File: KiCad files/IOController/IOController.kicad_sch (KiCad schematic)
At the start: 22 parts, among them J2 XT60 Horizontal Socket, J3 edge connector, Q1 BSS138, SW1 RotaryEncoder_Switch, SW2 B3U, U1 LP2985-1.8, U2 TLV75533PDBV, U3 LP2985-5.0, U4 RP2040

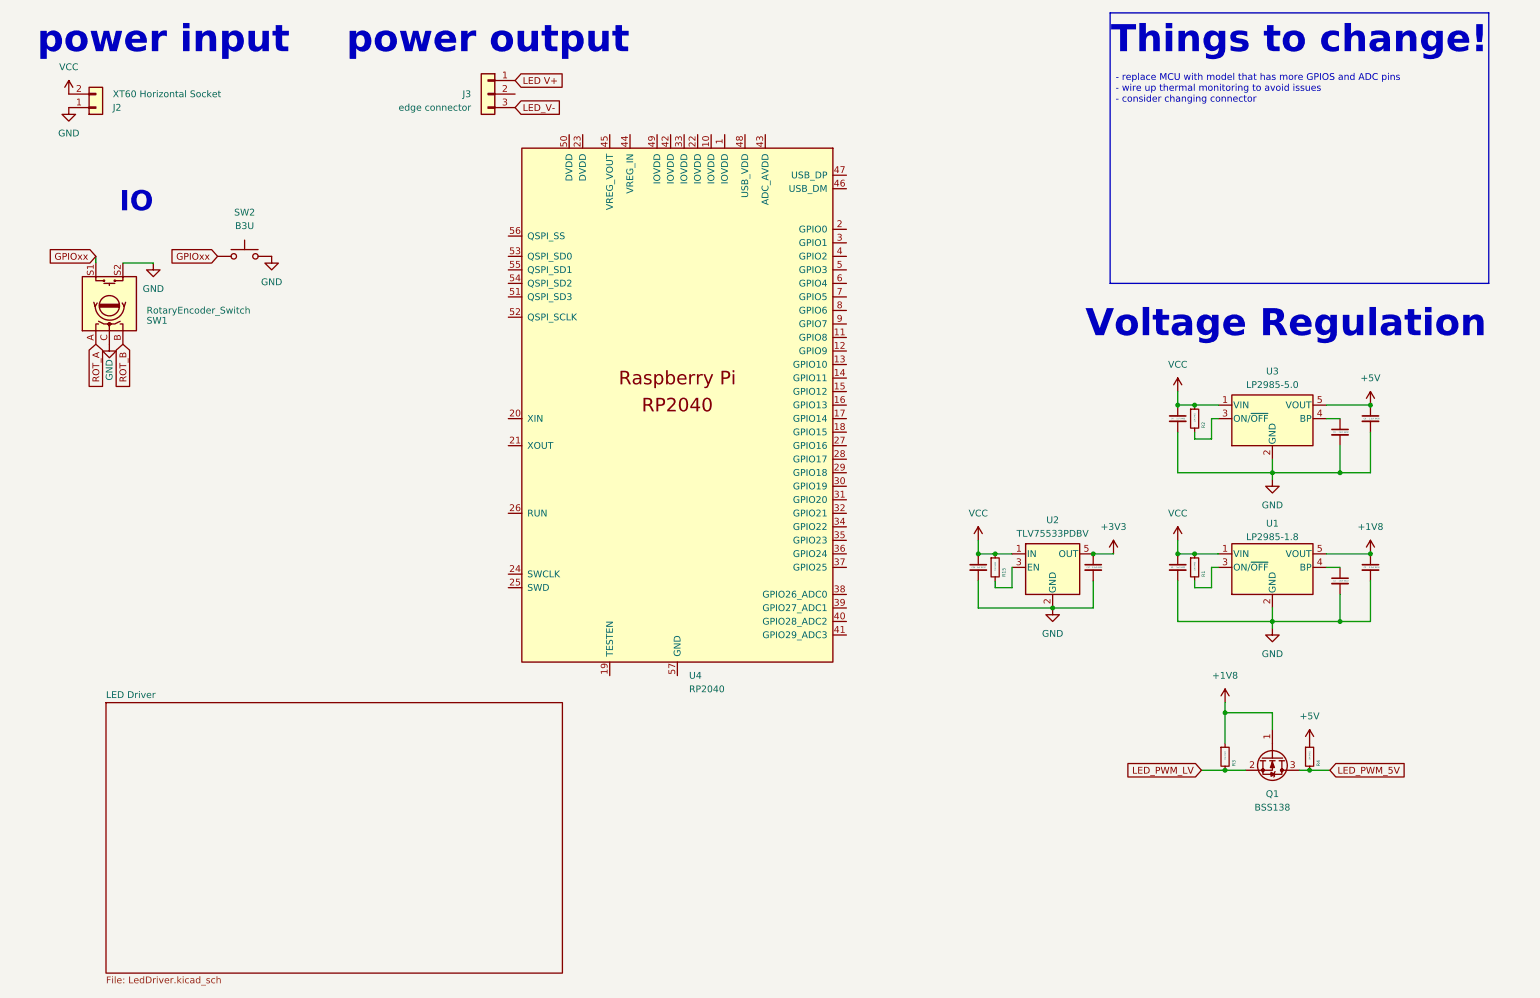
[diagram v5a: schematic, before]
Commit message: swapped RP2040 for attiny1634, still requires more work.
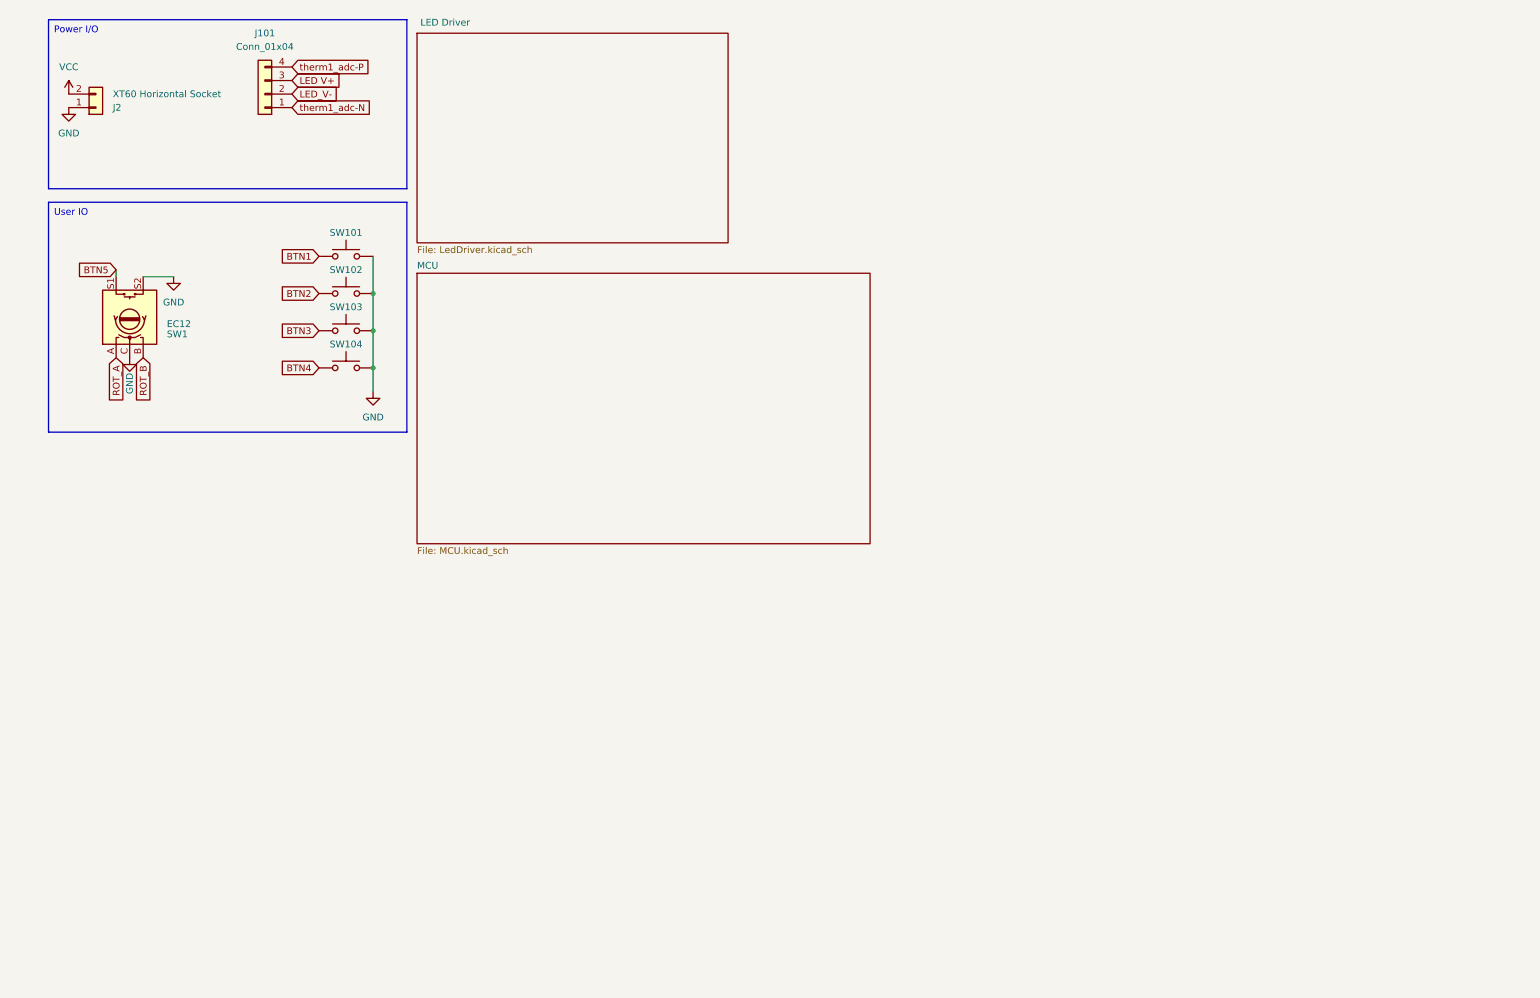
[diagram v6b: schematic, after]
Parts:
- removed C1, C26, C4: 1uF 0402, Capacitor_SMD:C_0402_1005Metric, symbol Device:C_Small
- removed C2, C5: 10nF 0402, Capacitor_SMD:C_0402_1005Metric, symbol Device:C_Small
- removed C27, C3, C6: 2.2uF 0402, Capacitor_SMD:C_0402_1005Metric, symbol Device:C_Small
- removed J3: edge connector, EnvExtras:CardEdge1x03, symbol Connector_Generic:Conn_01x03
- removed Q1: BSS138, Package_TO_SOT_SMD:SOT-23, symbol Transistor_FET:BSS138
- removed R1, R15, R2, R3, R4: 10K 0402, Resistor_SMD:R_0402_1005Metric, symbol Device:R_Small
- removed U1: LP2985-1.8, Package_TO_SOT_SMD:SOT-23-5, symbol Regulator_Linear:LP2985-1.8
- removed U2: TLV75533PDBV, Package_TO_SOT_SMD:SOT-23-5, symbol Regulator_Linear:TLV75533PDBV
- removed U3: LP2985-5.0, Package_TO_SOT_SMD:SOT-23-5, symbol Regulator_Linear:LP2985-1.8
- removed U4: RP2040, RP2040_minimal_r2:RP2040-QFN-56, symbol MCU_RaspberryPi_RP2040:RP2040
- added J101: Conn_01x04, Connector_Wire:SolderWire-0.5sqmm_1x04_P4.8mm_D0.9mm_OD2.3mm, symbol Connector_Generic:Conn_01x04
- added SW102, SW103, SW104: B3U, Button_Switch_SMD:SW_SPST_B3U-1000P-B, symbol Switch:SW_Push
- SW1: value RotaryEncoder_Switch -> EC12
- renumbered SW2 to SW101
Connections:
- net GND: now also SW102.2, SW103.2, SW104.2
- net LED V+: now also J101.3 (Pin_3)
- net LED_V-: now also J101.2 (Pin_2)
- net GPIOxx renamed BTN1
- net BTN1: no longer SW1.S1
- new net BTN2: SW102.1
- new net BTN3: SW103.1
- new net BTN4: SW104.1
- new net BTN5: SW1.S1
- new net therm1_adc-N: J101.1 (Pin_1)
- new net therm1_adc-P: J101.4 (Pin_4)
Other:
- added sheet MCU (MCU.kicad_sch)
- note removed: "IO"
- note removed: "Things to change!"
- note removed: "Voltage Regulation"
- note removed: "power input"
- note removed: "power output"
- moved on the sheet: SW1, SW101
